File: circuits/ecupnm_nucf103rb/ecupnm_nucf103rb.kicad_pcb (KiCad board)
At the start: 2 copper layers, 70.6 x 64.8 mm, 41 parts, among them J1 Conn_01x02_Pin, J2 Conn_01x02_Pin, J3 Conn_01x03_Pin, J4 USB_B_Mini, Q1 2N3904, Q2 IRF540N, Q3 IRF540N, U1 NUCLEO-64, U2 H11L1, U3 AMS1117-5.0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

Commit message: Nucleo Based
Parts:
- C5, R8: moved to F.Cu
- moved R14 5.09 mm to (147.3, 77.7), turned to 0 degrees
- moved JT1 5.02 mm to (105.1, 116.3)
- moved R1 5.02 mm to (108.4, 112.7)
- moved R2 5.02 mm to (113.5, 110.3)
- moved C1 5.02 mm to (113.5, 112.7)
- moved J1 5.02 mm to (108.9, 107.7)
- moved R12 2.07 mm to (128.3, 68.3), turned to -90 degrees
- moved R11 2.05 mm to (131.3, 77.5)
- moved R15 1.91 mm to (151.4, 67.8), turned to -90 degrees
- moved J4 1.88 mm to (126.7, 118.8)
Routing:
- net GND: track 47.6 -> 425.5 mm, vias 0 -> 8
- net VDD: track 19.0 -> 176.9 mm, vias 0 -> 6
- net VCC: track 0.00 -> 115.3 mm, vias 0 -> 4
- net GNDPWR: track 0.00 -> 82.3 mm, vias 0 -> 3
- net +12V: track 0.00 -> 77.1 mm, vias 0 -> 3
- net OUT_INJ: track 0.00 -> 61.6 mm, vias 0 -> 1
- net RX: track 0.00 -> 47.4 mm, vias 0 -> 1
- net TX: track 0.00 -> 34.8 mm, vias 0 -> 1
- net OUT_IGN: track 0.00 -> 28.2 mm, vias 0 -> 1
- net Net-(J4-D-): track 0.00 -> 14.9 mm
- net Net-(J4-D+): track 0.00 -> 13.6 mm
- net PORT_IGN: track 0.00 -> 12.1 mm
- net PORT_INJ: track 0.00 -> 11.3 mm
- net Net-(Q3-G): track 0.00 -> 8.33 mm
- net Net-(Q2-G): track 0.00 -> 7.70 mm
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- added copper zone on B.Cu, net (none)
- added copper zone on F.Cu, net (none)
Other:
- board text added: "Custom ECU"
- board text added: "Deny Nur, ST, MT"
- board text added: "USB DATA"

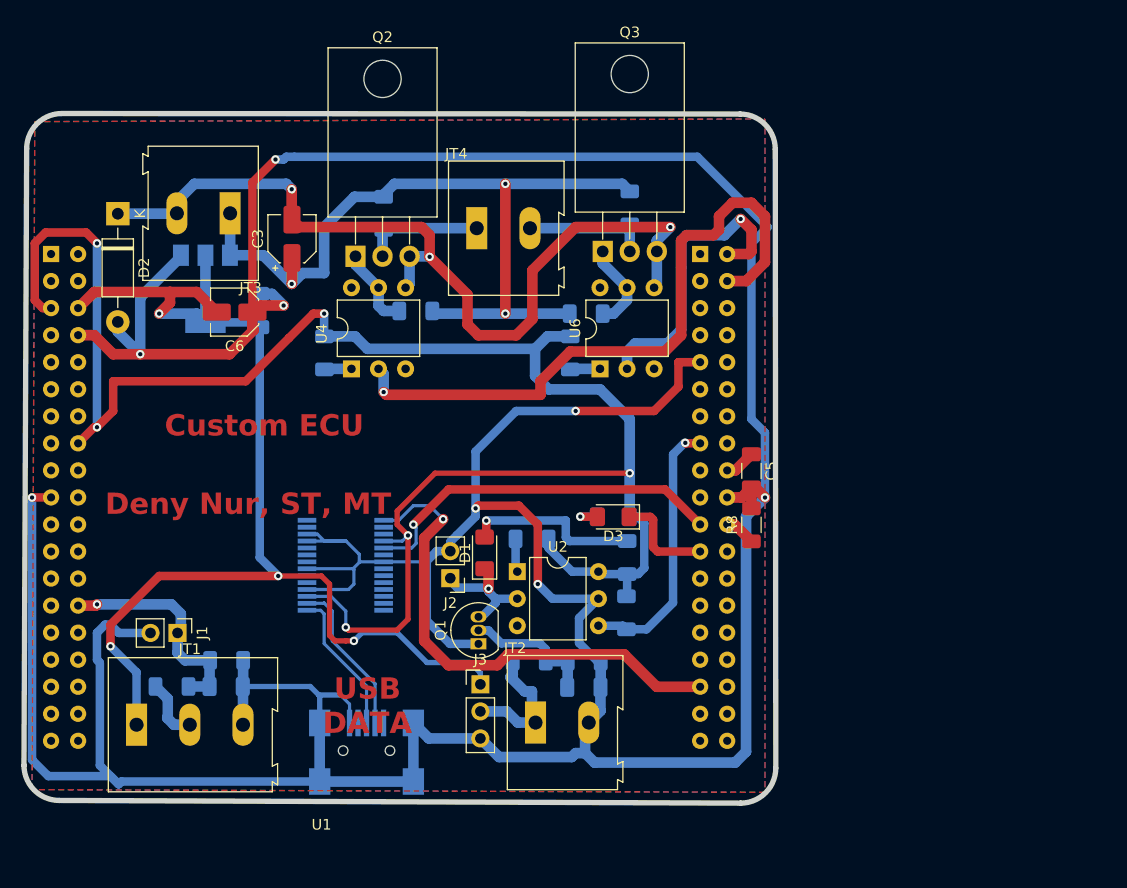
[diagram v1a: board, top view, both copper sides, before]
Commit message: Ganti Orientasi PCB ECU
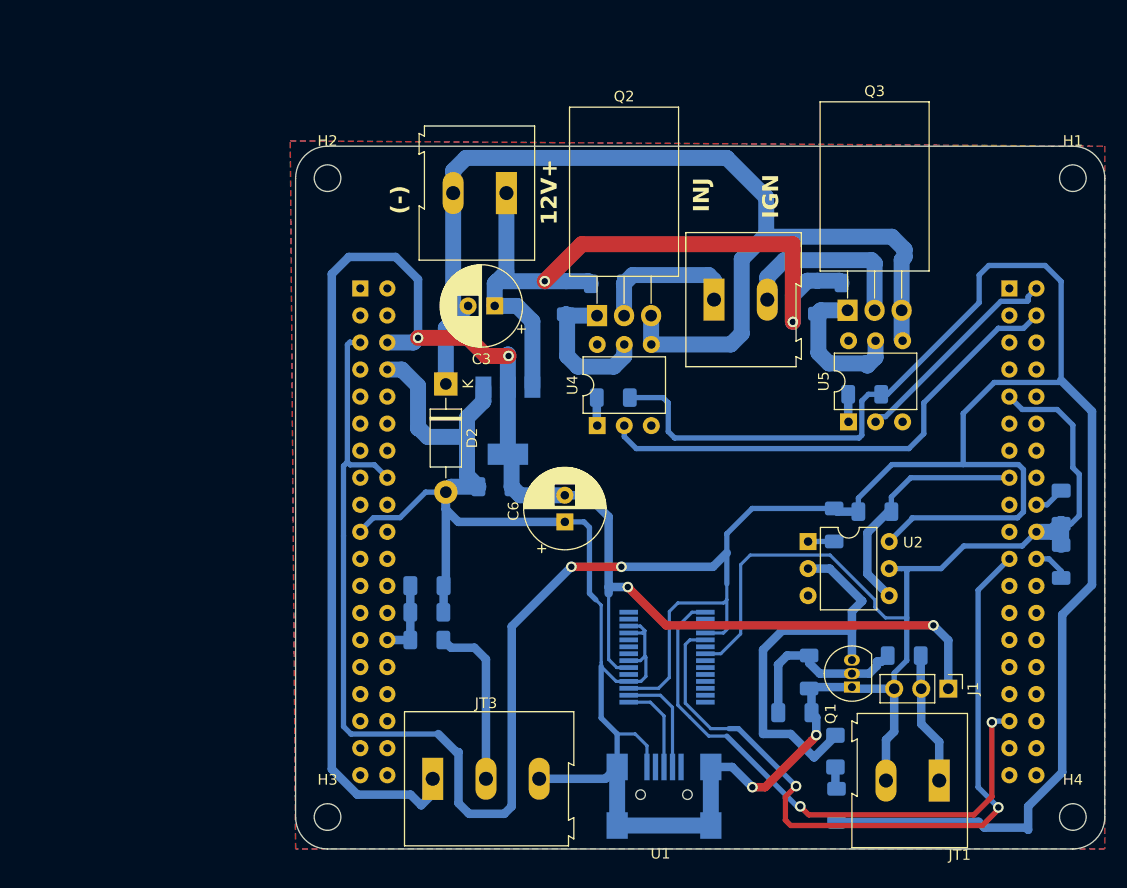
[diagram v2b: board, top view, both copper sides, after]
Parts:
- removed D3: LED, LED_SMD:LED_1206_3216Metric_Pad1.42x1.75mm_HandSolder
- removed J3: Conn_01x03_Pin, Connector_PinHeader_2.54mm:PinHeader_1x03_P2.54mm_Vertical
- removed J4: USB_B_Mini, Connector_USB:USB_Mini-B_Wuerth_65100516121_Horizontal
- removed R15: 10k, Resistor_SMD:R_1206_3216Metric_Pad1.30x1.75mm_HandSolder
- added H1: MountingHole, MountingHole:MountingHole_2.5mm, F.Cu at (193.0, 65.0)
- added H2: MountingHole, MountingHole:MountingHole_2.5mm, F.Cu at (123.0, 65.0)
- added H3: MountingHole, MountingHole:MountingHole_2.5mm, F.Cu at (123.0, 125.0)
- added H4: MountingHole, MountingHole:MountingHole_2.5mm, F.Cu at (193.0, 125.0)
- C2: value 100nF -> 4.7uF
- C3: footprint Capacitor_SMD:CP_Elec_4x5.4 -> Capacitor_THT:CP_Radial_D7.5mm_P2.50mm
- C5: value 4.7uF -> 100nF; moved to B.Cu
- C6: footprint Capacitor_SMD:C_Elec_4x5.4 -> Capacitor_THT:CP_Radial_D7.5mm_P2.50mm
- D1: moved to B.Cu
- J1: value Conn_01x02_Pin -> Conn_01x03_Pin; footprint Connector_PinHeader_2.54mm:PinHeader_1x02_P2.54mm_Vertical -> Connector_PinHeader_2.54mm:PinHeader_1x03_P2.54mm_Vertical
- J2: value Conn_01x02_Pin -> USB_B_Mini; footprint Connector_PinHeader_2.54mm:PinHeader_1x02_P2.54mm_Vertical -> Connector_USB:USB_Mini-B_Wuerth_65100516121_Horizontal; moved to B.Cu
- JT1: value Conn_01x03_Pin -> Conn_01x02_Pin; footprint TerminalBlock:TerminalBlock_Altech_AK300-3_P5.00mm -> TerminalBlock:TerminalBlock_Altech_AK300-2_P5.00mm
- JT3: value Conn_01x02_Pin -> Conn_01x03_Pin; footprint TerminalBlock:TerminalBlock_Altech_AK300-2_P5.00mm -> TerminalBlock:TerminalBlock_Altech_AK300-3_P5.00mm
- R10, R13: value 220 -> 10k
- R12: value 10k -> 220
- R2: value 1k -> 10k
- R3: value 1k -> 330
- R4: value 10k -> 330
- R5: value 330 -> 10K
- R6: value 330 -> 0
- R7: value 10K -> 1k
- R8: value 0 -> 1k; moved to B.Cu
- U5: value FT232RL -> 4N35; footprint Package_SO:SSOP-28_5.3x10.2mm_P0.65mm -> Package_DIP:DIP-6_W7.62mm; moved to F.Cu
- U6: value 4N35 -> FT232RL; footprint Package_DIP:DIP-6_W7.62mm -> Package_SO:SSOP-28_5.3x10.2mm_P0.65mm; moved to B.Cu
- moved JT1 75.6 mm to (180.4, 121.6), turned to 180 degrees
- moved J1 72.6 mm to (181.3, 113.0)
- moved R1 68.8 mm to (177.2, 109.8), turned to 180 degrees
- moved JT3 56.4 mm to (132.9, 121.4), turned to 0 degrees
- moved R2 54.7 mm to (168.2, 111.4), turned to -90 degrees
- moved C1 53.5 mm to (166.9, 115.2)
- moved JT2 49.8 mm to (139.8, 66.4), turned to 180 degrees
- moved R6 49.7 mm to (191.9, 101.0), turned to 90 degrees
- moved U5 49.1 mm to (171.9, 87.9), turned to 90 degrees
- moved R12 48.3 mm to (173.4, 85.3), turned to 180 degrees
- moved C2 47.9 mm to (191.9, 95.9), turned to -90 degrees
- moved D1 37.8 mm to (170.7, 118.8), turned to -90 degrees
- moved C6 36.7 mm to (145.3, 97.3), turned to 90 degrees
- moved Q1 35.3 mm to (172.2, 112.8)
- moved D2 34.7 mm to (134.1, 84.3)
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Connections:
- C1 pad 2: IN_TPS -> Net-(Q1-B)
- C2 pad 1: GND -> Net-(U1B-PB11/VCAP)
- C2 pad 2: Net-(Q1-B) -> GND
- C4 pad 2: VCC -> IN_TPS
- C5 pad 1: Net-(U1B-PB11/VCAP) -> GND
- C5 pad 2: GND -> VCC
- J1 pad 1: IN_TPS -> VCC
- J1 pad 2: GND -> PULSER
- J2 pad 1: IN_PULSE -> unconnected-(J2-VBUS-Pad1)
- J2 pad 2: GND -> Net-(J2-D-)
- JT1 pad 1: VCC -> PULSER
- JT1 pad 2: Net-(JT1-Pin_2) -> GND
- JT2 pad 1: PULSER -> +12V
- JT2 pad 2: GND -> GNDPWR
- JT3 pad 1: +12V -> VCC
- JT3 pad 2: GNDPWR -> Net-(JT3-Pin_2)
- R1 pad 1: Net-(JT1-Pin_2) -> PULSER
- R1 pad 2: IN_TPS -> Net-(Q1-B)
- R10 pad 1: VDD -> +12V
- R10 pad 2: Net-(R10-Pad2) -> Net-(Q2-G)
- R11 pad 2: Net-(Q2-G) -> PORT_INJ
- R12 pad 1: +12V -> VDD
- R12 pad 2: PORT_INJ -> Net-(R12-Pad2)
- R13 pad 1: VDD -> +12V
- R13 pad 2: Net-(R13-Pad2) -> Net-(Q3-G)
- R14 pad 2: Net-(Q3-G) -> PORT_IGN
- R2 pad 1: GND -> Net-(Q1-B)
- R2 pad 2: IN_TPS -> GND
- R3 pad 1: PULSER -> VDD
- R3 pad 2: Net-(Q1-B) -> Net-(D1-A)
- R4 pad 1: Net-(Q1-B) -> VDD
- R4 pad 2: GND -> Net-(R4-Pad2)
- R5 pad 2: Net-(D1-A) -> IN_CKP
- R6 pad 1: VDD -> Net-(U1B-PB2)
- R6 pad 2: Net-(R6-Pad2) -> GND
- R7 pad 1: VDD -> Net-(JT3-Pin_2)
- R7 pad 2: IN_CKP -> IN_TPS
- R8 pad 1: Net-(U1B-PB2) -> GND
- R8 pad 2: GND -> IN_TPS
- R9 pad 2: Net-(D3-A) -> Net-(R9-Pad2)
- U1 pad 61: LED_NOCKP -> unconnected-(U1B-PA8-Pad61)
- U2 pad 1: Net-(R6-Pad2) -> Net-(R4-Pad2)
- U4 pad 1: Net-(R10-Pad2) -> Net-(R9-Pad2)
- U5 pad 1: RX -> Net-(R12-Pad2)
- U5 pad 2: unconnected-(U5-DTR-Pad2) -> OUT_IGN
- U5 pad 4: VDD -> GNDPWR
- U5 pad 5: TX -> Net-(Q3-G)
- U6 pad 1: Net-(R13-Pad2) -> RX
- U6 pad 2: OUT_IGN -> unconnected-(U6-DTR-Pad2)
- U6 pad 4: GNDPWR -> VDD
- U6 pad 5: Net-(Q3-G) -> TX
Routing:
- net GND: track 425.5 -> 247.1 mm, vias 8 -> 2
- net VDD: track 176.9 -> 324.1 mm, vias 6 -> 2
- net VCC: track 115.3 -> 163.8 mm
- net TX: track 34.8 -> 71.2 mm, vias 1 -> 2
- net IN_PULSE: track 12.0 -> 38.1 mm, vias 1 -> 0
- net GNDPWR: track 82.3 -> 102.5 mm, vias 3 -> 0
- net Net-(JT3-Pin_2): track 0.00 -> 16.0 mm
- net Net-(J4-D-): track 14.9 -> 0.00 mm
- net OUT_INJ: track 61.6 -> 47.1 mm, vias 1 -> 0
- net IN_TPS: track 21.7 -> 7.26 mm, vias 1 -> 0
- net Net-(D1-A): track 16.6 -> 2.20 mm, vias 1 -> 0
- net Net-(J4-D+): track 13.6 -> 0.00 mm
- net Net-(J2-D-): track 0.00 -> 10.2 mm
- net LED_NOCKP: track 9.53 -> 0.00 mm
- net Net-(J2-D+): track 0.00 -> 8.65 mm
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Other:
- board size 70.6 x 64.8 mm -> 76 x 66 mm
- board text added: "(-)"
- board text added: "12V+"
- board text added: "IGN"
- board text added: "INJ"
- board text removed: "Custom ECU"
- board text removed: "Deny Nur, ST, MT"
- board text removed: "USB DATA"
